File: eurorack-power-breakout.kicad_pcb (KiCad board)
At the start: 2 copper layers, 22.9 x 53.3 mm, 23 parts, among them J1 upper, J2 lower, J3 bus, J4 PWR, SW1 SW_SPDT

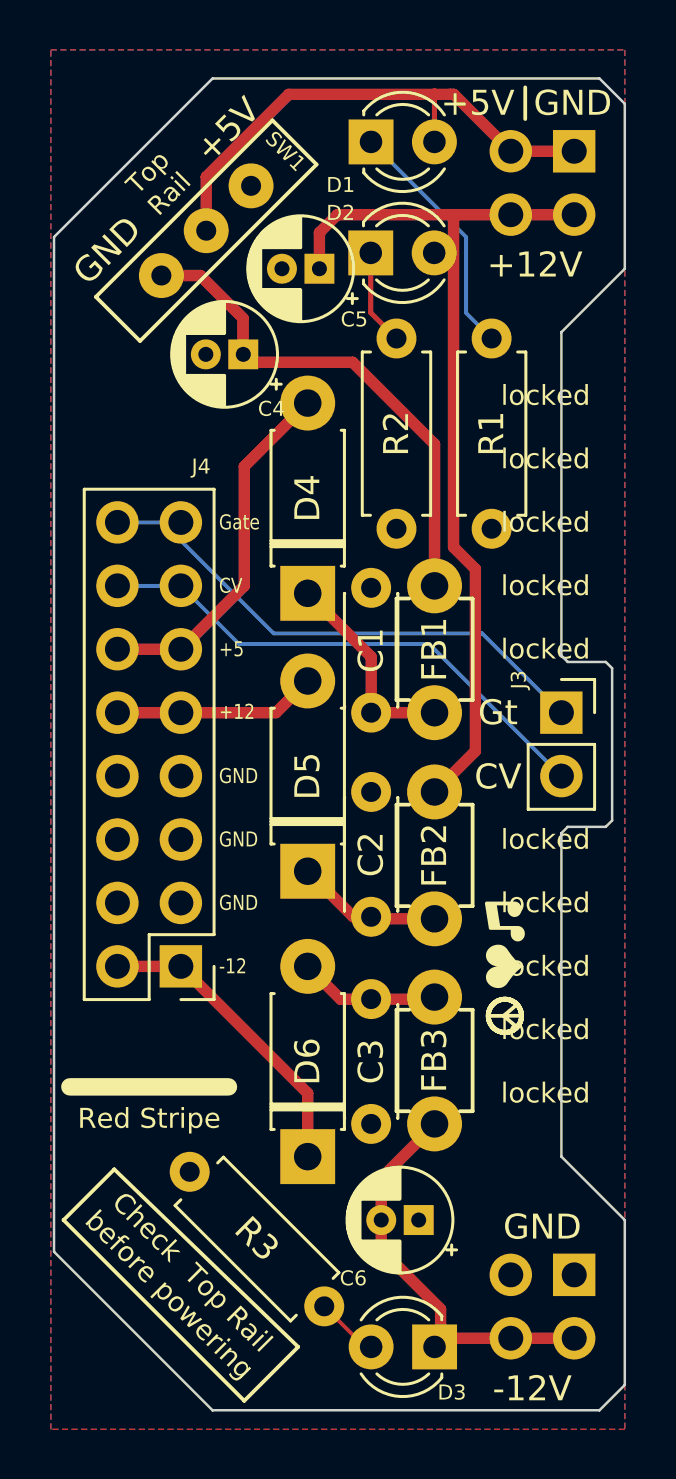
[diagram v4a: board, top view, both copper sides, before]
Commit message: Adapt PCB to schematic changes
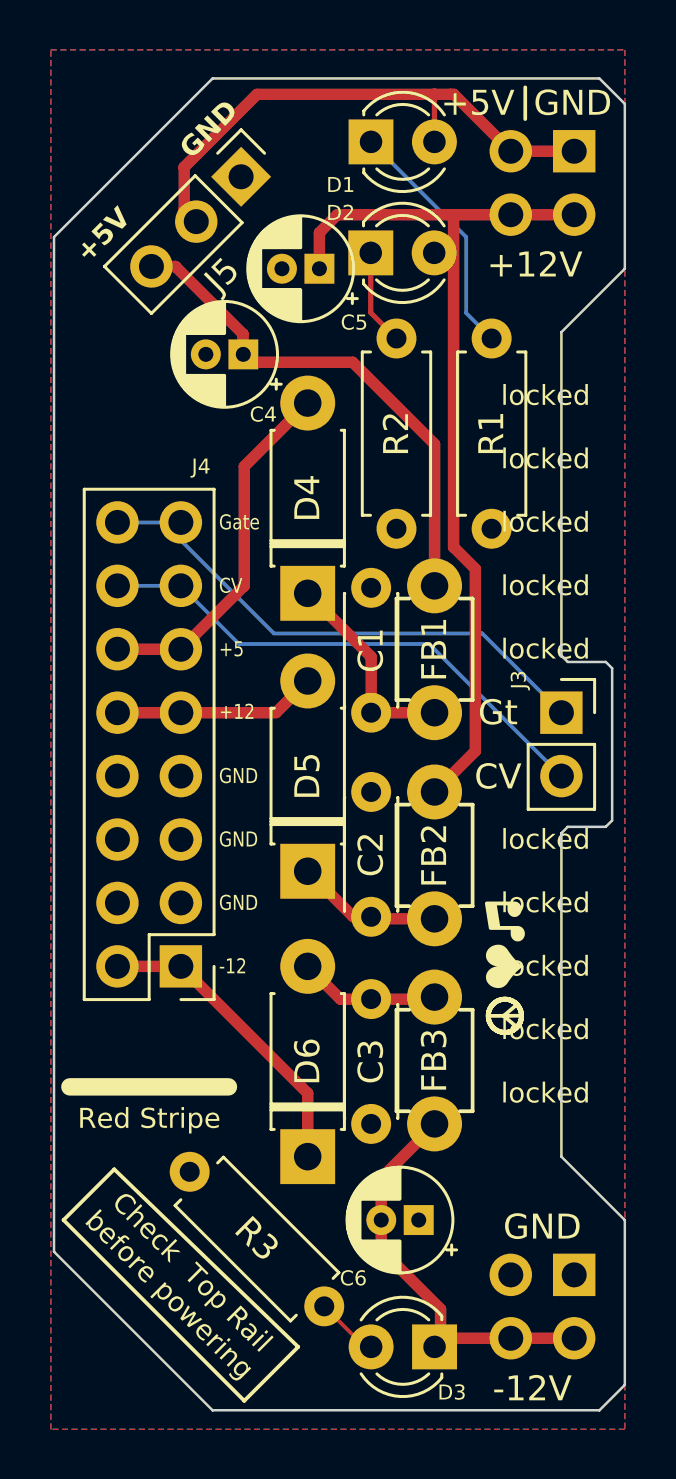
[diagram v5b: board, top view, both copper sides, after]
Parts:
- removed SW1: SW_SPDT, mopsy:Switch_SPDT_NK236
- added J5: Conn_01x03, Connector_PinHeader_2.54mm:PinHeader_1x03_P2.54mm_Vertical, F.Cu at (134.5, 87.8)
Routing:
- net 5Vselect: track 21.1 -> 22.1 mm
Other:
- board text removed: "Top Rail"
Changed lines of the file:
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@@
     (property "ki_keywords" "cap capacitor")
     (attr through_hole)
-    (fp_text reference "C5" (at -1.397 -2.032) (layer "F.SilkS")
+    (fp_text reference "C5" (at -1.397 -2.159) (layer "F.SilkS")
         (effects (font (size 0.6 0.6) (thickness 0.1)))
     )
@@
     )
   )
-  (footprint "mopsy:Switch_SPDT_NK236" (layer "F.Cu")
-    (at 133.096 89.916 45)
-    (property "REICHELT" "NK 236")
+  (footprint "Connector_PinHeader_2.54mm:PinHeader_1x03_P2.54mm_Vertical" (layer "F.Cu")
+    (at 134.493 87.757 -45)
+    (descr "Through hole straight pin header, 1x03, 2.54mm pitch, single row")
+    (tags "Through hole pin header THT 1x03 2.54mm single row")
     (property "Sheetfile" "eurorack-power-breakout.kicad_sch")
     (property "Sheetname" "")
-    (property "ki_description" "Switch, single pole double throw")
-    (property "ki_keywords" "switch single-pole double-throw spdt ON-ON")
+    (property "ki_description" "Generic connector, single row, 01x03, script generated (kicad-library-utils/schlib/autogen/connector/)")
+    (property "ki_keywords" "connector")
     (attr through_hole)
-    (fp_text reference "SW1" (at 4.490128 0 315 unlocked) (layer "F.SilkS")
-        (effects (font (size 0.6 0.6) (thickness 0.1)))
-    )
-    (fp_text value "SW_SPDT" (at 0 2.032 45 unlocked) (layer "F.Fab")
-        (effects (font (size 1 1) (thickness 0.15)))
-    )
-    (fp_line (start -5 -1.25) (end -5 1.25)
-      (stroke (width 0.15) (type solid)) (layer "F.SilkS"))
-    (fp_line (start -5 -1.25) (end 5 -1.25)
-      (stroke (width 0.15) (type solid)) (layer "F.SilkS"))
-    (fp_line (start -5 1.25) (end 5 1.25)
-      (stroke (width 0.15) (type solid)) (layer "F.SilkS"))
-    (fp_line (start 5 -1.25) (end 5 1.25)
-      (stroke (width 0.15) (type solid)) (layer "F.SilkS"))
-    (pad "1" thru_hole circle (at 0 0 45) (size 1.8 1.8) (drill 0.8) (layers "*.Cu" "*.Mask")
-      (net 13 "5Vselect") (pinfunction "B") (pintype "passive"))
-    (pad "2" thru_hole circle (at 2.54 0 45) (size 1.8 1.8) (drill 0.8) (layers "*.Cu" "*.Mask")
-      (net 2 "GND") (pinfunction "A") (pintype "passive"))
-    (pad "3" thru_hole circle (at -2.54 0 45) (size 1.8 1.8) (drill 0.8) (layers "*.Cu" "*.Mask")
-      (net 5 "+5V") (pinfunction "C") (pintype "passive"))
+    (fp_text reference "J5" (at 2.245064 3.322695 -135) (layer "F.SilkS")
+        (effects (font (size 1 1) (thickness 0.15)))
+    )
+    (fp_text value "Conn_01x03" (at 0 7.41 135) (layer "F.Fab")
+        (effects (font (size 1 1) (thickness 0.15)))
+    )
+    (fp_text user "${REFERENCE}" (at 0 2.54 45) (layer "F.Fab")
+        (effects (font (size 1 1) (thickness 0.15)))
+    )
+    (fp_line (start -1.33 -1.33) (end 0 -1.33)
+      (stroke (width 0.12) (type solid)) (layer "F.SilkS"))
+    (fp_line (start -1.33 0) (end -1.33 -1.33)
+      (stroke (width 0.12) (type solid)) (layer "F.SilkS"))
+    (fp_line (start -1.33 1.27) (end -1.33 6.41)
+      (stroke (width 0.12) (type solid)) (layer "F.SilkS"))
+    (fp_line (start -1.33 1.27) (end 1.33 1.27)
+      (stroke (width 0.12) (type solid)) (layer "F.SilkS"))
+    (fp_line (start -1.33 6.41) (end 1.33 6.41)
+      (stroke (width 0.12) (type solid)) (layer "F.SilkS"))
+    (fp_line (start 1.33 1.27) (end 1.33 6.41)
+      (stroke (width 0.12) (type solid)) (layer "F.SilkS"))
+    (fp_line (start -1.8 -1.8) (end -1.8 6.85)
+      (stroke (width 0.05) (type solid)) (layer "F.CrtYd"))
+    (fp_line (start -1.8 6.85) (end 1.8 6.85)
+      (stroke (width 0.05) (type solid)) (layer "F.CrtYd"))
+    (fp_line (start 1.8 -1.8) (end -1.8 -1.8)
+      (stroke (width 0.05) (type solid)) (layer "F.CrtYd"))
+    (fp_line (start 1.8 6.85) (end 1.8 -1.8)
+      (stroke (width 0.05) (type solid)) (layer "F.CrtYd"))
+    (fp_line (start -1.27 -0.635) (end -0.635 -1.27)
+      (stroke (width 0.1) (type solid)) (layer "F.Fab"))
+    (fp_line (start -1.27 6.35) (end -1.27 -0.635)
+      (stroke (width 0.1) (type solid)) (layer "F.Fab"))
+    (fp_line (start -0.635 -1.27) (end 1.27 -1.27)
+      (stroke (width 0.1) (type solid)) (layer "F.Fab"))
+    (fp_line (start 1.27 -1.27) (end 1.27 6.35)
+      (stroke (width 0.1) (type solid)) (layer "F.Fab"))
+    (fp_line (start 1.27 6.35) (end -1.27 6.35)
+      (stroke (width 0.1) (type solid)) (layer "F.Fab"))
+    (pad "1" thru_hole rect (at 0 0 315) (size 1.7 1.7) (drill 1) (layers "*.Cu" "*.Mask")
+      (net 2 "GND") (pinfunction "Pin_1") (pintype "passive"))
+    (pad "2" thru_hole oval (at 0 2.54 315) (size 1.7 1.7) (drill 1) (layers "*.Cu" "*.Mask")
+      (net 13 "5Vselect") (pinfunction "Pin_2") (pintype "passive"))
+    (pad "3" thru_hole oval (at 0 5.08 315) (size 1.7 1.7) (drill 1) (layers "*.Cu" "*.Mask")
+      (net 5 "+5V") (pinfunction "Pin_3") (pintype "passive"))
+    (model "${KICAD6_3DMODEL_DIR}/Connector_PinHeader_2.54mm.3dshapes/PinHeader_1x03_P2.54mm_Vertical.wrl"
+      (offset (xyz 0 0 0))
+      (scale (xyz 1 1 1))
+      (rotate (xyz 0 0 0))
+    )
   )
   (footprint "Diode_THT:D_DO-41_SOD81_P7.62mm_Horizontal" (layer "F.Cu")
@@
     (property "ki_keywords" "cap capacitor")
     (attr through_hole)
-    (fp_text reference "C4" (at -1.131 -2.1844) (layer "F.SilkS")
+    (fp_text reference "C4" (at -0.8014 -2.413) (layer "F.SilkS")
         (effects (font (size 0.6 0.6) (thickness 0.1)))
     )
@@
     (effects (font (size 0.6 0.5) (thickness 0.1)) (justify left))
   )
+  (gr_text "GND" (at 134.493 85.217 45) (layer "F.SilkS")
+    (effects (font (size 0.8 0.8) (thickness 0.15) bold) (justify right bottom))
+  )
   (gr_text "GND" (at 147.7772 84.8106) (layer "F.SilkS")
     (effects (font (size 1 1) (thickness 0.15)))
   )
-  (gr_text "Top\nRail" (at 131.191 88.011 45) (layer "F.SilkS")
-    (effects (font (size 0.75 0.75) (thickness 0.125)))
-  )
-  (gr_text "+5V" (at 135.001 84.836 45) (layer "F.SilkS")
-    (effects (font (size 1 1) (thickness 0.15)) (justify right))
-  )
   (gr_text "-12V" (at 146.1516 136.2964) (layer "F.SilkS")
     (effects (font (size 1 1) (thickness 0.15)))
@@
     (effects (font (size 0.6 0.5) (thickness 0.1)) (justify left))
   )
-  (gr_text "GND" (at 128.016 91.821 45) (layer "F.SilkS")
-    (effects (font (size 1 1) (thickness 0.15)) (justify left))
-  )
   (gr_text locked "E" (at 146.685 106.68) (layer "F.SilkS")
     (effects (font (size 0.8 0.8) (thickness 0.15)))
@@
   (gr_text locked "G" (at 146.685 116.84) (layer "F.SilkS")
     (effects (font (size 0.8 0.8) (thickness 0.15)))
+  )
+  (gr_text "+5V" (at 128.397 91.313 45) (layer "F.SilkS")
+    (effects (font (size 0.8 0.8) (thickness 0.15) bold) (justify left bottom))
   )
   (gr_text locked "J" (at 146.685 124.46) (layer "F.SilkS")
@@
   (segment (start 138.47 120.69) (end 137.16 119.38) (width 0.4572) (layer "F.Cu") (net 4))
   (segment (start 142.16 120.69) (end 142.24 120.61) (width 0.4572) (layer "F.Cu") (net 4))
-  (segment (start 131.299949 91.712051) (end 132.860051 91.712051) (width 0.4572) (layer "F.Cu") (net 5))
-  (segment (start 134.5684 95.1866) (end 138.961423 95.1866) (width 0.4572) (layer "F.Cu") (net 5))
-  (segment (start 138.961423 95.1866) (end 142.24 98.465177) (width 0.4572) (layer "F.Cu") (net 5))
-  (segment (start 132.860051 91.712051) (end 134.5684 93.4204) (width 0.4572) (layer "F.Cu") (net 5))
-  (segment (start 142.24 98.465177) (end 142.24 104.14) (width 0.4572) (layer "F.Cu") (net 5))
-  (segment (start 134.5684 93.4204) (end 134.5684 95.1866) (width 0.4572) (layer "F.Cu") (net 5))
+  (segment (start 142.24 104.14) (end 142.24 98.465177) (width 0.4572) (layer "F.Cu") (net 5))
+  (segment (start 138.961423 95.1866) (end 134.5684 95.1866) (width 0.4572) (layer "F.Cu") (net 5))
+  (segment (start 131.862102 91.349102) (end 130.900898 91.349102) (width 0.4572) (layer "F.Cu") (net 5))
+  (segment (start 134.5684 94.0554) (end 131.862102 91.349102) (width 0.4572) (layer "F.Cu") (net 5))
+  (segment (start 142.24 98.465177) (end 138.961423 95.1866) (width 0.4572) (layer "F.Cu") (net 5))
+  (segment (start 134.5684 95.1866) (end 134.5684 94.0554) (width 0.4572) (layer "F.Cu") (net 5))
   (segment (start 142.24 112.395) (end 143.8734 110.7616) (width 0.4572) (layer "F.Cu") (net 6))
   (segment (start 145.293 89.275) (end 143.135 89.275) (width 0.4572) (layer "F.Cu") (net 6))
@@
   (segment (start 132.08 109.22) (end 135.89 109.22) (width 0.4572) (layer "F.Cu") (net 12))
   (segment (start 129.54 109.22) (end 132.08 109.22) (width 0.4572) (layer "F.Cu") (net 12))
-  (segment (start 133.096 89.916) (end 133.096 87.761866) (width 0.4572) (layer "F.Cu") (net 13))
-  (segment (start 133.096 87.761866) (end 136.402866 84.455) (width 0.4572) (layer "F.Cu") (net 13))
+  (segment (start 132.207 87.376) (end 132.207 89.063102) (width 0.4572) (layer "F.Cu") (net 13))
+  (segment (start 132.207 89.063102) (end 132.696949 89.553051) (width 0.4572) (layer "F.Cu") (net 13))
+  (segment (start 135.128 84.455) (end 132.207 87.376) (width 0.4572) (layer "F.Cu") (net 13))
   (segment (start 147.833 86.735) (end 145.293 86.735) (width 0.4572) (layer "F.Cu") (net 13))
-  (segment (start 136.402866 84.455) (end 142.24 84.455) (width 0.4572) (layer "F.Cu") (net 13))
   (segment (start 142.24 84.455) (end 142.235 84.46) (width 0.4572) (layer "F.Cu") (net 13))
   (segment (start 142.235 86.36) (end 142.235 84.46) (width 0.2032) (layer "F.Cu") (net 13))
+  (segment (start 142.24 84.455) (end 135.128 84.455) (width 0.4572) (layer "F.Cu") (net 13))
   (segment (start 145.293 86.735) (end 143.013 84.455) (width 0.4572) (layer "F.Cu") (net 13))
   (segment (start 143.013 84.455) (end 142.875 84.455) (width 0.4572) (layer "F.Cu") (net 13))
@@
     )
   )
-  (group "" (id 328a3e07-e919-466a-ba37-5dcbd587bbaa)
-    (members
-      2433a415-cccf-47cb-b92e-a6df7b3b5b29
-      34a7ac5c-71e3-4539-9024-c5e5a928339d
-      616f80a0-df34-4eeb-ac04-ad06a7ae1ddd
-      a37a2192-4fdb-4eed-aa01-6a753eeadaff
-    )
-  )

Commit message: Change URL to moPsy website
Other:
- board text added: "https://www.mopsy-music.de/tools/eurorackpowerbreakout"
- board text removed: "https://github.com/moPsy-project/eurorack-power-breakout"
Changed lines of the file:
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@@
   (gr_rect (start 126.746 97.155) (end 134.874 123.952)
     (stroke (width 0.05) (type solid)) (fill none) (layer "F.CrtYd"))
-  (gr_text "v1.1" (at 136.398 134.874 90) (layer "B.SilkS")
+  (gr_text "v1.1" (at 135.89 134.747 90) (layer "B.SilkS")
     (effects (font (size 0.8 0.8) (thickness 0.1)) (justify right mirror))
   )
-  (gr_text "https://github.com/moPsy-project/eurorack-power-breakout" (at 134.62 134.62 90) (layer "B.SilkS")
+  (gr_text "https://www.mopsy-music.de/tools/eurorackpowerbreakout" (at 134.62 134.62 90) (layer "B.SilkS")
     (effects (font (size 0.8 0.8) (thickness 0.1)) (justify right mirror))
   )

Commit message: Add the moPsiOct label
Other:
- board text added: "moPsiOct"
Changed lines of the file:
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@@
   (gr_rect (start 126.746 97.155) (end 134.874 123.952)
     (stroke (width 0.05) (type solid)) (fill none) (layer "F.CrtYd"))
-  (gr_text "v1.1" (at 135.89 134.747 90) (layer "B.SilkS")
+  (gr_text "v1.1" (at 136.017 133.096 90) (layer "B.SilkS")
     (effects (font (size 0.8 0.8) (thickness 0.1)) (justify right mirror))
   )
-  (gr_text "https://www.mopsy-music.de/tools/eurorackpowerbreakout" (at 134.62 134.62 90) (layer "B.SilkS")
+  (gr_text "https://www.mopsy-music.de/tools/eurorackpowerbreakout" (at 134.747 132.969 90) (layer "B.SilkS")
     (effects (font (size 0.8 0.8) (thickness 0.1)) (justify right mirror))
   )
@@
     (effects (font (size 0.6 0.6) (thickness 0.1)) (justify mirror))
   )
+  (gr_text "moPsiOct" (at 133.35 135.763 -45) (layer "B.SilkS")
+    (effects (font (size 1 1) (thickness 0.15)) (justify left bottom mirror))
+  )
   (gr_text locked "D" (at 146.685 104.14) (layer "F.SilkS")
